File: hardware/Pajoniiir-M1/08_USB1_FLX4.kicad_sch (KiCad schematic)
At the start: 9 parts

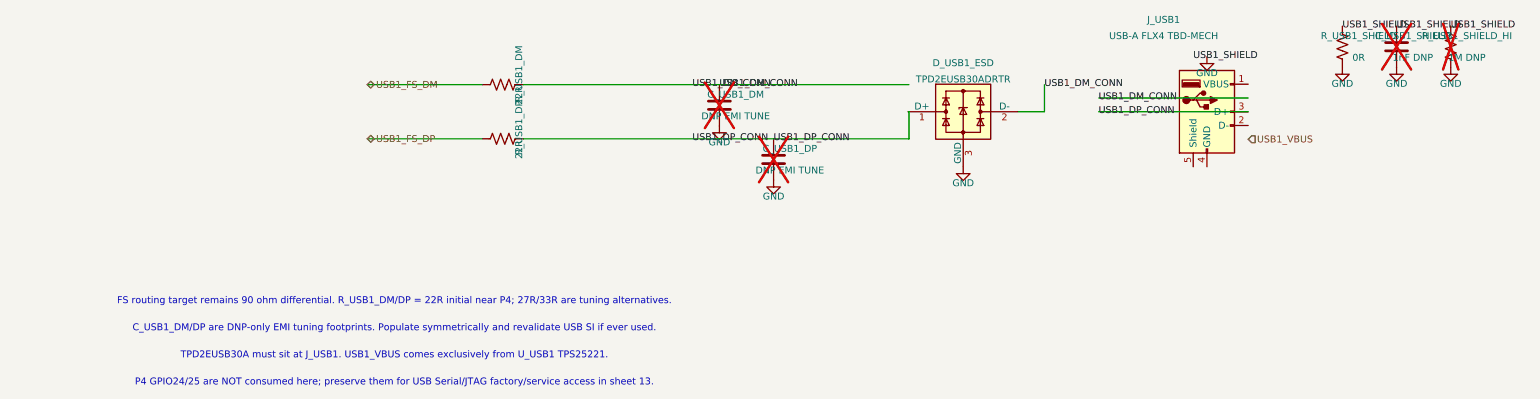
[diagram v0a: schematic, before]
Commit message: hardware: snap child sheets 06-10 to 25 mil grid
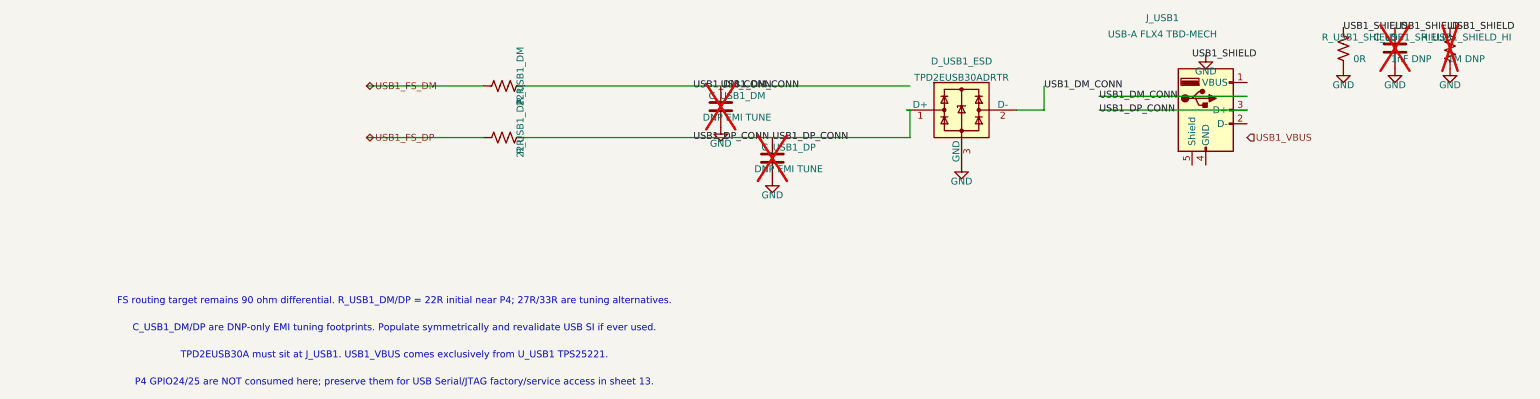
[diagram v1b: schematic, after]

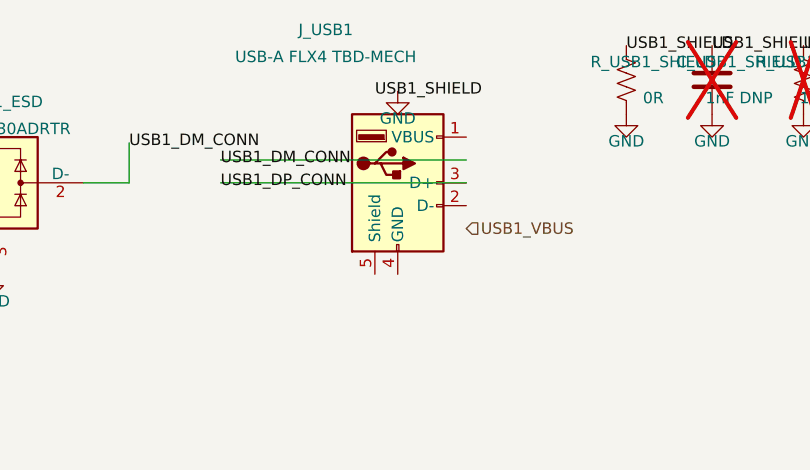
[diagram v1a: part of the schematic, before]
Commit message: hardware: correct USB-A connector pin mapping
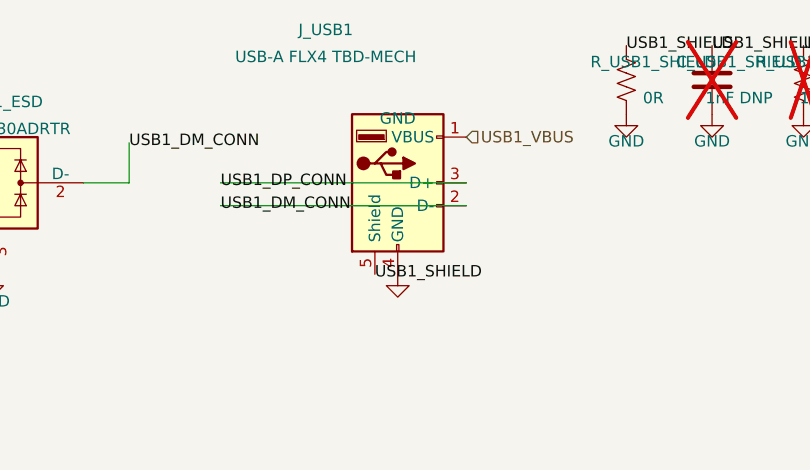
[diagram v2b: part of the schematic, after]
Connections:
- net GND: now also J_USB1.4 (GND)
- net USB1_DM_CONN: now also J_USB1.2 (D-)
- net USB1_SHIELD: now also J_USB1.5 (Shield)
- net USB1_VBUS: now also J_USB1.1 (VBUS)
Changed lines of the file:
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@@
     (instances (project "Pajoniiir-M1" (path "/2c8dd352-b7b8-4d9e-8f93-5dd43be2a100/31000008-6b2a-4a3a-8c91-000000000008" (reference "J_USB1") (unit 1))))
   )
-  (hierarchical_label "USB1_VBUS" (shape input) (at 192.405 64.77 0) (effects (font (size 1.27 1.27))))
-  (wire (pts (xy 192.405 57.15) (xy 165.1 57.15)) (stroke (width 0) (type default)))
-  (label "USB1_DM_CONN" (at 165.1 57.15 0) (effects (font (size 1.27 1.27))))
+  (hierarchical_label "USB1_VBUS" (shape input) (at 192.405 54.61 0) (effects (font (size 1.27 1.27))))
+  (wire (pts (xy 192.405 62.23) (xy 165.1 62.23)) (stroke (width 0) (type default)))
+  (label "USB1_DM_CONN" (at 165.1 62.23 0) (effects (font (size 1.27 1.27))))
   (wire (pts (xy 192.405 59.69) (xy 165.1 59.69)) (stroke (width 0) (type default)))
   (label "USB1_DP_CONN" (at 165.1 59.69 0) (effects (font (size 1.27 1.27))))
   (symbol
-    (lib_id "power:GND") (at 184.785 49.53 0) (unit 1)
+    (lib_id "power:GND") (at 184.785 69.85 0) (unit 1)
     (exclude_from_sim no) (in_bom yes) (on_board yes) (dnp no)
     (property "Reference" "#PWR0804" (at 184.785 55.53 0) (effects (font (size 1.27 1.27)) (hide yes)))
@@
     (instances (project "Pajoniiir-M1" (path "/2c8dd352-b7b8-4d9e-8f93-5dd43be2a100/31000008-6b2a-4a3a-8c91-000000000008" (reference "#PWR0804") (unit 1))))
   )
-  (label "USB1_SHIELD" (at 182.245 49.53 0) (effects (font (size 1.27 1.27))))
+  (label "USB1_SHIELD" (at 182.245 69.85 0) (effects (font (size 1.27 1.27))))
   (symbol
     (lib_id "Device:R_US") (at 210.185 48.26 0) (unit 1)

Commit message: hardware: declare verified rail power sources for ERC
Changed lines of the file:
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@@
   (text "TPD2EUSB30A must sit at J_USB1. USB1_VBUS comes exclusively from U_USB1 TPS25221." (exclude_from_sim no) (at 35 105 0) (effects (font (size 1.27 1.27))))
   (text "P4 GPIO24/25 are NOT consumed here; preserve them for USB Serial/JTAG factory/service access in sheet 13." (exclude_from_sim no) (at 35 110 0) (effects (font (size 1.27 1.27))))
+  (symbol
+    (lib_id "power:PWR_FLAG")
+    (at 192.405 54.61 0)
+    (unit 1)
+    (exclude_from_sim no)
+    (in_bom yes)
+    (on_board yes)
+    (dnp no)
+    (property "Reference" "#FLG0801" (at 192.405 56.515 0) (effects (font (size 1.27 1.27)) (hide yes)))
+    (property "Value" "PWR_FLAG" (at 192.405 58.42 0) (effects (font (size 1.27 1.27))))
+    (property "Footprint" "" (at 192.405 54.61 0) (effects (font (size 1.27 1.27)) (hide yes)))
+    (property "Datasheet" "~" (at 192.405 54.61 0) (effects (font (size 1.27 1.27)) (hide yes)))
+    (property "Description" "Special symbol for telling ERC where power comes from" (at 192.405 54.61 0) (effects (font (size 1.27 1.27)) (hide yes)))
+    (pin "1")
+    (instances (project "Pajoniiir-M1" (path "/2c8dd352-b7b8-4d9e-8f93-5dd43be2a100/31000008-6b2a-4a3a-8c91-000000000008" (reference "#FLG0801") (unit 1))))
+  )
   (sheet_instances (path "/" (page "9")))
   (embedded_fonts no)
